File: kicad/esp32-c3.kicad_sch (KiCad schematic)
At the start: 19 parts, among them U1 SN65HVD230, U5 ESP32-C3-MINI-1

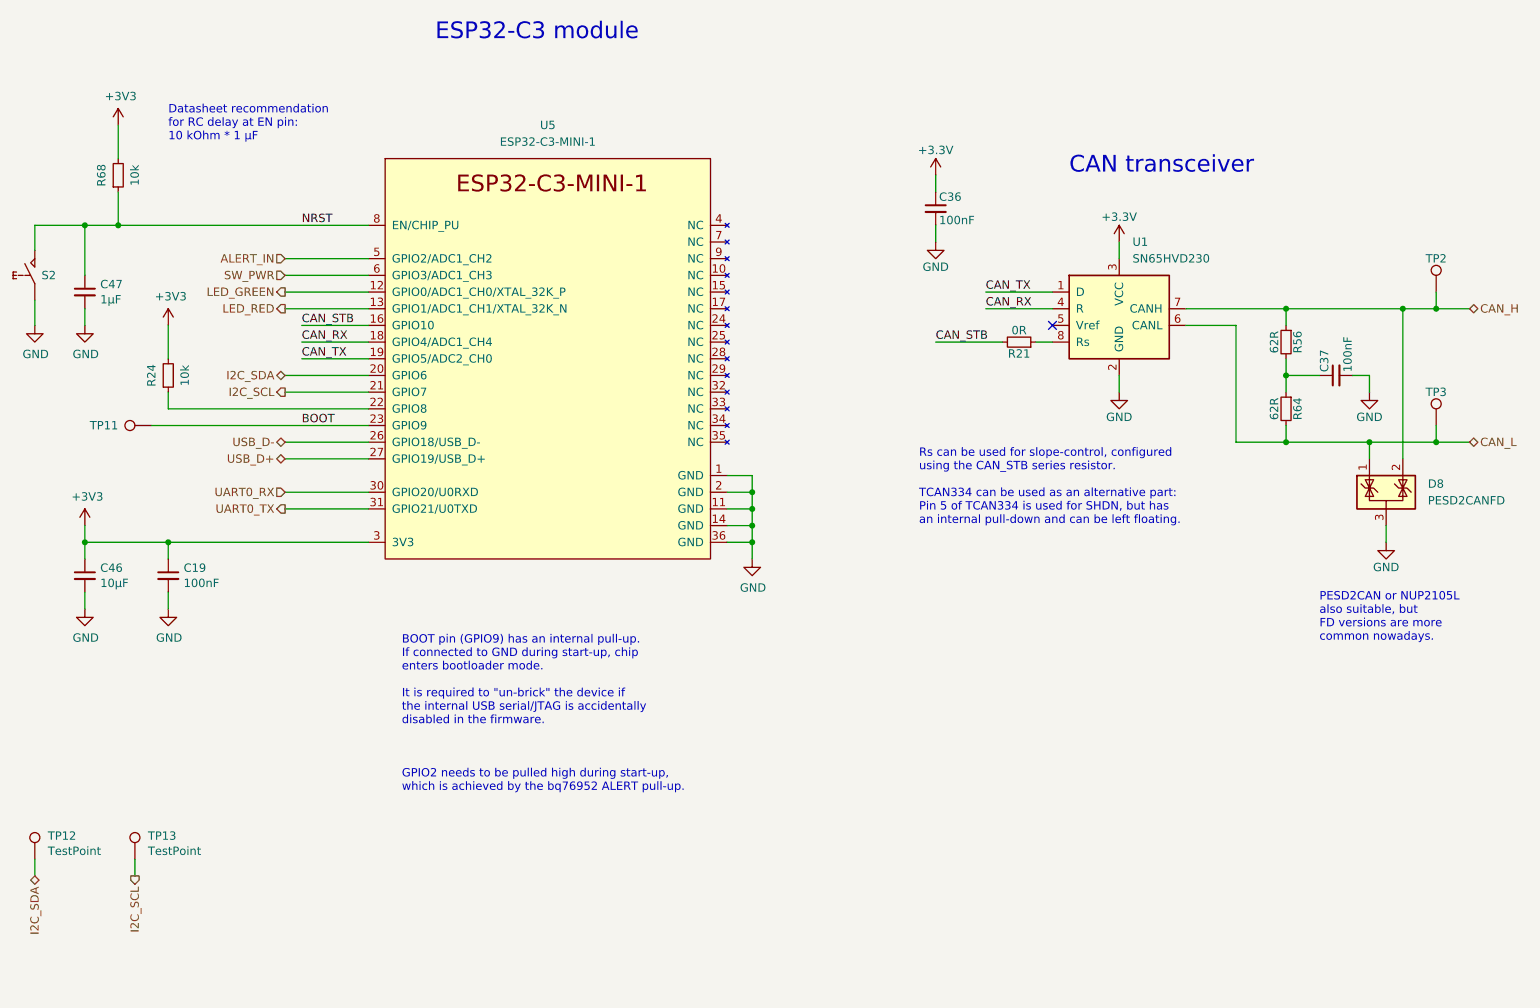
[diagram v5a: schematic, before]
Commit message: v0.4.0: Multiple improvements for new board revision
- Use LMR38010 for internal power supply (max. 80V instead of 60V)
- Change USB connector from Micro-A to C and remove 5V power supply
  which was not working anyway. The board cannot be powered by USB
  only.
- Add TS2 (connected to DFETOFF) to measure shunt temperature
- Add RS-485 transceiver (sharing the connector with CAN)
- Switch I2C pins of ESP32-C3 to GPIO8/9. This allows to re-use the
  I2C pull-ups for strapping configuration and frees two pins for the
  RS-485 transceiver RE and DE pins. Also we may get rid of the I2C
  glitches during start-up.
- Use 80V instead of 100V power MOSFETs to reduce Rds(on).
- Reduce DSG gate resistor R57 to 47R to increase switch-off speed.
- Adjust some resistors to reduce number of different parts
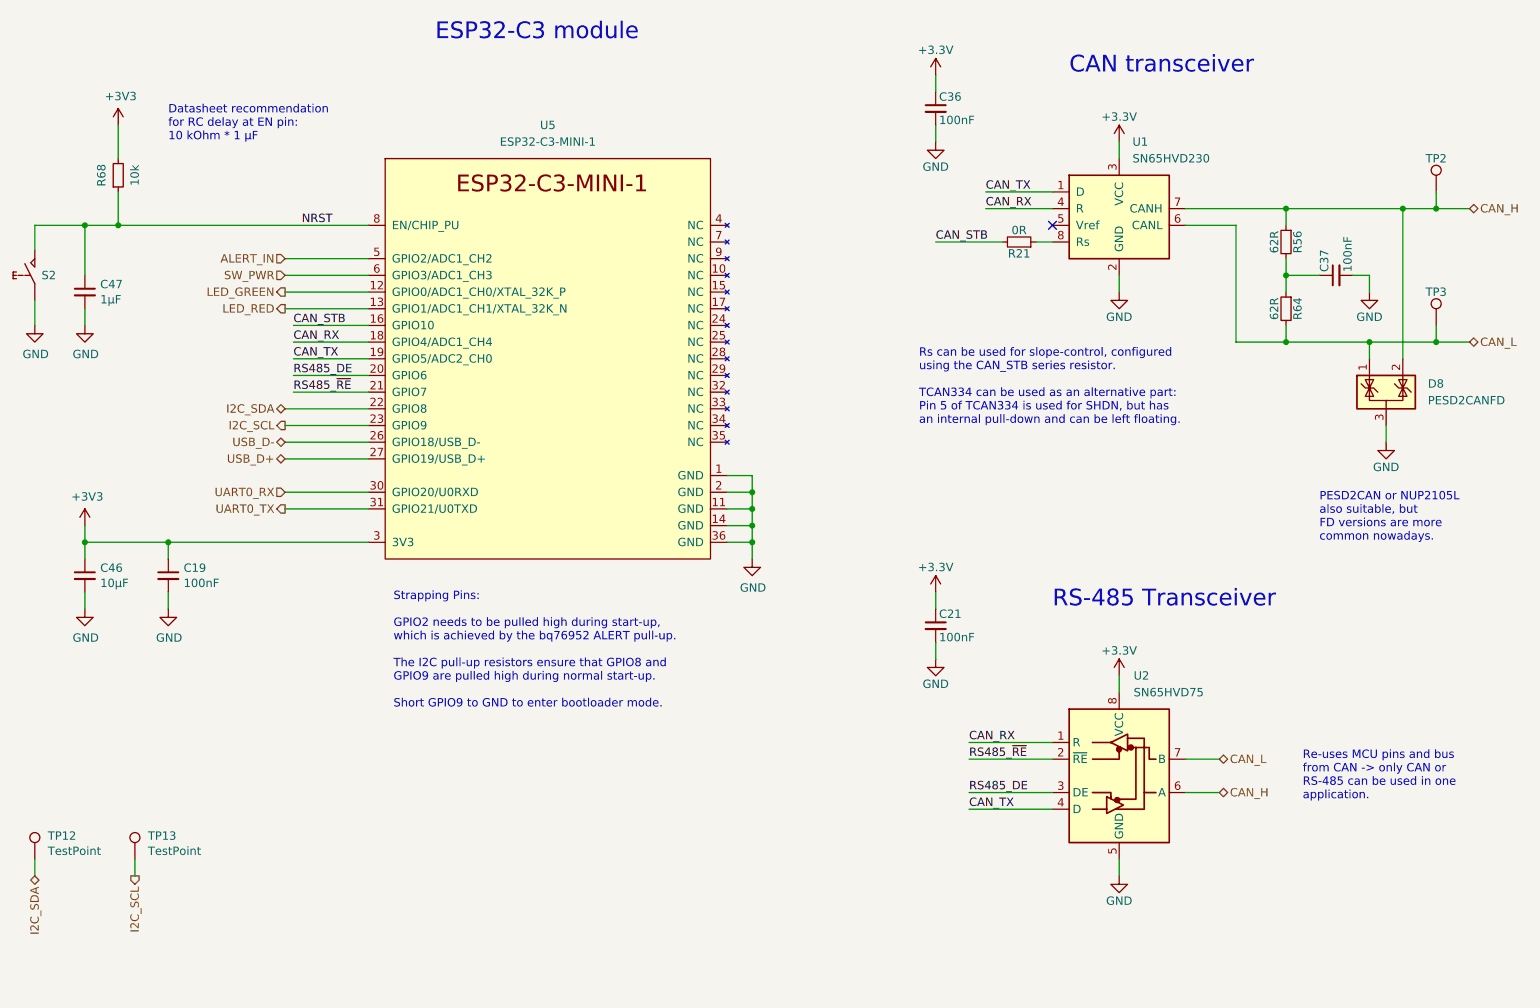
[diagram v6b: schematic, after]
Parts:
- removed R24: 10k, LibreSolar:R_0603_1608, symbol LibreSolar:R
- removed TP11: TestPoint, TestPoint:TestPoint_Pad_D1.5mm, symbol Connector:TestPoint
- added C21: 100nF, LibreSolar:C_0603_1608, symbol LibreSolar:C
- added U2: SN65HVD75, Package_SO:SOIC-8_3.9x4.9mm_P1.27mm, symbol Interface_UART:SN65HVD11HD
- C19, C36, C37: LCSC (none) -> C15725; Manufacturer any -> Samsung Electro-Mechanics; PartNumber (none) -> CL10B104KC8NNNC; Remarks X7R, 100V -> min. 100V, X7R
- C46: LCSC (none) -> C17024; Manufacturer Murata -> Samsung Electro-Mechanics; PartNumber GRM21BR61E106KA73L -> CL21A106KPFNNNE; Remarks 25V, X5R -> min. 10V, X5R
- C47: LCSC (none) -> C5673; Manufacturer any -> Samsung Electro-Mechanics; PartNumber (none) -> CL10A105KA8NNNC; Remarks (none) -> min. 10V, X5R
- D8: LCSC (none) -> C552486
- R21: Manufacturer any -> Yageo; PartNumber (none) -> RC0603FR-070RL
- R56, R64: Manufacturer any -> Yageo; PartNumber (none) -> RC0603FR-0762RL
- R68: Manufacturer any -> Yageo; PartNumber (none) -> RC0603FR-0710KL
- U1: LCSC (none) -> C12084; PartNumber SN65HVD230D -> SN65HVD230DR
- U5: LCSC (none) -> C2838502
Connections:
- net BOOT is gone; now on net I2C_SCL: U5.23 (GPIO9)
- net +3V3: now also C21.1, U2.8 (VCC)
- net CAN_H: now also U2.6 (A)
- net CAN_L: now also U2.7 (B)
- net CAN_RX: now also U2.1 (R)
- net CAN_TX: now also U2.4 (D)
- net GND: now also C21.2, U2.5 (GND)
- net I2C_SCL: no longer U5.21 (GPIO7)
- net I2C_SDA: now also U5.22 (GPIO8); no longer U5.20 (GPIO6)
- new net RS485_DE: U2.3 (DE), U5.20 (GPIO6)
- new net RS485_~{RE}: U2.2 (~{RE}), U5.21 (GPIO7)
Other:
- note added: "RS-485 Transceiver"
- note added: "Re-uses MCU pins and bus from CAN -> only CAN or RS-485 can be used in one application."
- note added: "Strapping Pins: GPIO2 needs to be pulled high during start-up, which is achieved by the bq76952 ALERT pull-up. The I2C pull-up resistors ensure that GPIO8 and GPIO9 are pulled high during normal start-up. Short GPIO9 to GND to enter bootloader mode."
- note removed: "BOOT pin (GPIO9) has an internal pull-up. If connected to GND during start-up, chip enters bootloader mode. It is required to "un-brick" the device if the internal USB serial/JTAG is accidentally disabled in the firmware."
- note removed: "GPIO2 needs to be pulled high during start-up, which is achieved by the bq76952 ALERT pull-up."
- moved on the sheet: C36, C37, D8, R21, R56, R64, TP2, TP3, U1

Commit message: Update files to KiCad v8
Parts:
- S2: LCSC (none) -> C2886899
